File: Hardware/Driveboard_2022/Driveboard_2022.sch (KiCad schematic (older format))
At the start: 10 parts, among them U1 TM4C129E_Launchpad

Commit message: Basically Finished
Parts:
- added Conn? (x12): Molex_SL_03, symbol MRDT_Connectors:Molex_SL_03
- added D? (x7): Blue, symbol Device:LED
- added LED? (x12): Yellow, symbol Device:LED
- added R? (x12): 500, symbol Device:R
- added R? (x7): 330, symbol Device:R
- added SW? (x6): SW_Push, symbol Switch:SW_Push
- added SW?: SW_SPST, symbol Switch:SW_SPST
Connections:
- net +3V3: now also Conn?.1, Conn?.1, Conn?.1, Conn?.1, Conn?.1, Conn?.1, SW?.1, SW?.1, SW?.1, SW?.1, SW?.1, SW?.1, SW?.1 (A)
- net GND: now also Conn?.2, Conn?.2, Conn?.2, Conn?.2, Conn?.2, Conn?.2, Conn?.2, Conn?.2, Conn?.2, Conn?.2, Conn?.2, Conn?.2, D?.1 (K), D?.1 (K), D?.1 (K), D?.1 (K), D?.1 (K), D?.1 (K), D?.1 (K), LED?.1 (K), LED?.1 (K), LED?.1 (K), LED?.1 (K), LED?.1 (K), LED?.1 (K), LED?.1 (K), LED?.1 (K), LED?.1 (K), LED?.1 (K), LED?.1 (K), LED?.1 (K)
- net FLRX: now reaches U1.PC4 (A1_3)
- net FLRX: now also Conn?.3, R?.1
- net FLTX: now reaches U1.PC5 (A1_4)
- net FLTX: now also Conn?.1, R?.1
- net MLRX: now reaches U1.PC6 (A1_5)
- net MLRX: now also Conn?.3, R?.1
- net MLTX: now reaches U1.PC7 (A1_8)
- net MLTX: now also Conn?.1, R?.1
- net BRRX: now reaches U1.PA6 (B1_8)
- net BRRX: now also Conn?.3, R?.1
- net FL_PWM: now reaches U1.PF1 (C1_1)
- net FL_PWM: now also Conn?.3
- net FR_PWM: now reaches U1.PF2 (C1_2)
- net FR_PWM: now also Conn?.3
- net ML_PWM: now reaches U1.PF3 (C1_3)
- net ML_PWM: now also Conn?.3
- net MR_PWM: now reaches U1.PG0 (C1_4)
- net MR_PWM: now also Conn?.3
- net BL_PWM: now reaches U1.PL4 (C1_5)
- net BL_PWM: now also Conn?.3
- net BR_PWM: now reaches U1.PL5 (C1_6)
- net BR_PWM: now also Conn?.3
- net DIR_SWITCH: now reaches U1.PP2 (D1_10)
- net DIR_SWITCH: now also R?.2, SW?.2 (B)
- net FRRX: now reaches U1.PP0 (A2_3)
- net FRRX: now also Conn?.3, R?.1
- net FRTX: now reaches U1.PP1 (A2_4)
- net FRTX: now also Conn?.1, R?.1
- net BLRX: now reaches U1.PA4 (B2_9)
- net BLRX: now also Conn?.3, R?.1
- net BLTX: now reaches U1.PA5 (B2_10)
- net BLTX: now also Conn?.1, R?.1
- net MRRX: now reaches U1.PK0 (B2_5)
- net MRRX: now also Conn?.3, R?.1
- net MRTX: now reaches U1.PK1 (B2_6)
- net MRTX: now also Conn?.1, R?.1
- net FL_DRIVE: now reaches U1.PG1 (C2_1)
- net FL_DRIVE: now also R?.2, SW?.2
- net FR_DRIVE: now reaches U1.PK4 (C2_2)
- net FR_DRIVE: now also R?.2, SW?.2
- net ML_DRIVE: now reaches U1.PK5 (C2_3)
- net ML_DRIVE: now also R?.2, SW?.2
- net MR_DRIVE: now reaches U1.PM0 (C2_4)
- net MR_DRIVE: now also R?.2, SW?.2
- net BL_DRIVE: now reaches U1.PM1 (C2_5)
- net BL_DRIVE: now also R?.2, SW?.2
- net BR_DRIVE: now reaches U1.PM2 (C2_6)
- net BR_DRIVE: now also R?.2, SW?.2
- net BRTX: now reaches U1.PA7 (D2_4)
- net BRTX: now also Conn?.1, R?.1
- new net: LED?.2 (A), R?.2 (x12)
- new net: D?.2 (A), R?.1 (x7)
- no-connect marks 2 -> 49
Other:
- moved on the sheet: LED1, LED2, R1, R2, U1G, U1H

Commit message: I did something guys
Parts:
- added LED? (x5): Blue, symbol Device:LED
- added LED?: Yellow, symbol Device:LED
- added R? (x6): 330, symbol Device:R
- LED? (x12): value Yellow -> Blue
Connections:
- net BL_PWM: now also R?.1
- net BR_PWM: now also R?.1
- net FL_PWM: now also R?.1
- net FR_PWM: now also R?.1
- net GND: now also LED?.1 (K), LED?.1 (K), LED?.1 (K), LED?.1 (K), LED?.1 (K), LED?.1 (K)
- net ML_PWM: now also R?.1
- net MR_PWM: now also R?.1
- new net: LED?.2 (A), R?.2 (x6)

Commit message: I DID MORE SHIT
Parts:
- added LED? (x6): Red, symbol Device:LED
- added R? (x6): 330, symbol Device:R
- LED?: value Yellow -> Blue
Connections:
- net GND: now also LED?.1 (K), LED?.1 (K), LED?.1 (K), LED?.1 (K), LED?.1 (K), LED?.1 (K)
- new net: LED?.2 (A), R?.2 (x6)
- new net BL_FLT: R?.1
- new net BR_FLT: R?.1
- new net FL_FLT: R?.1
- new net FR_FLT: R?.1
- new net ML_FLT: R?.1
- new net MR_FLT: R?.1

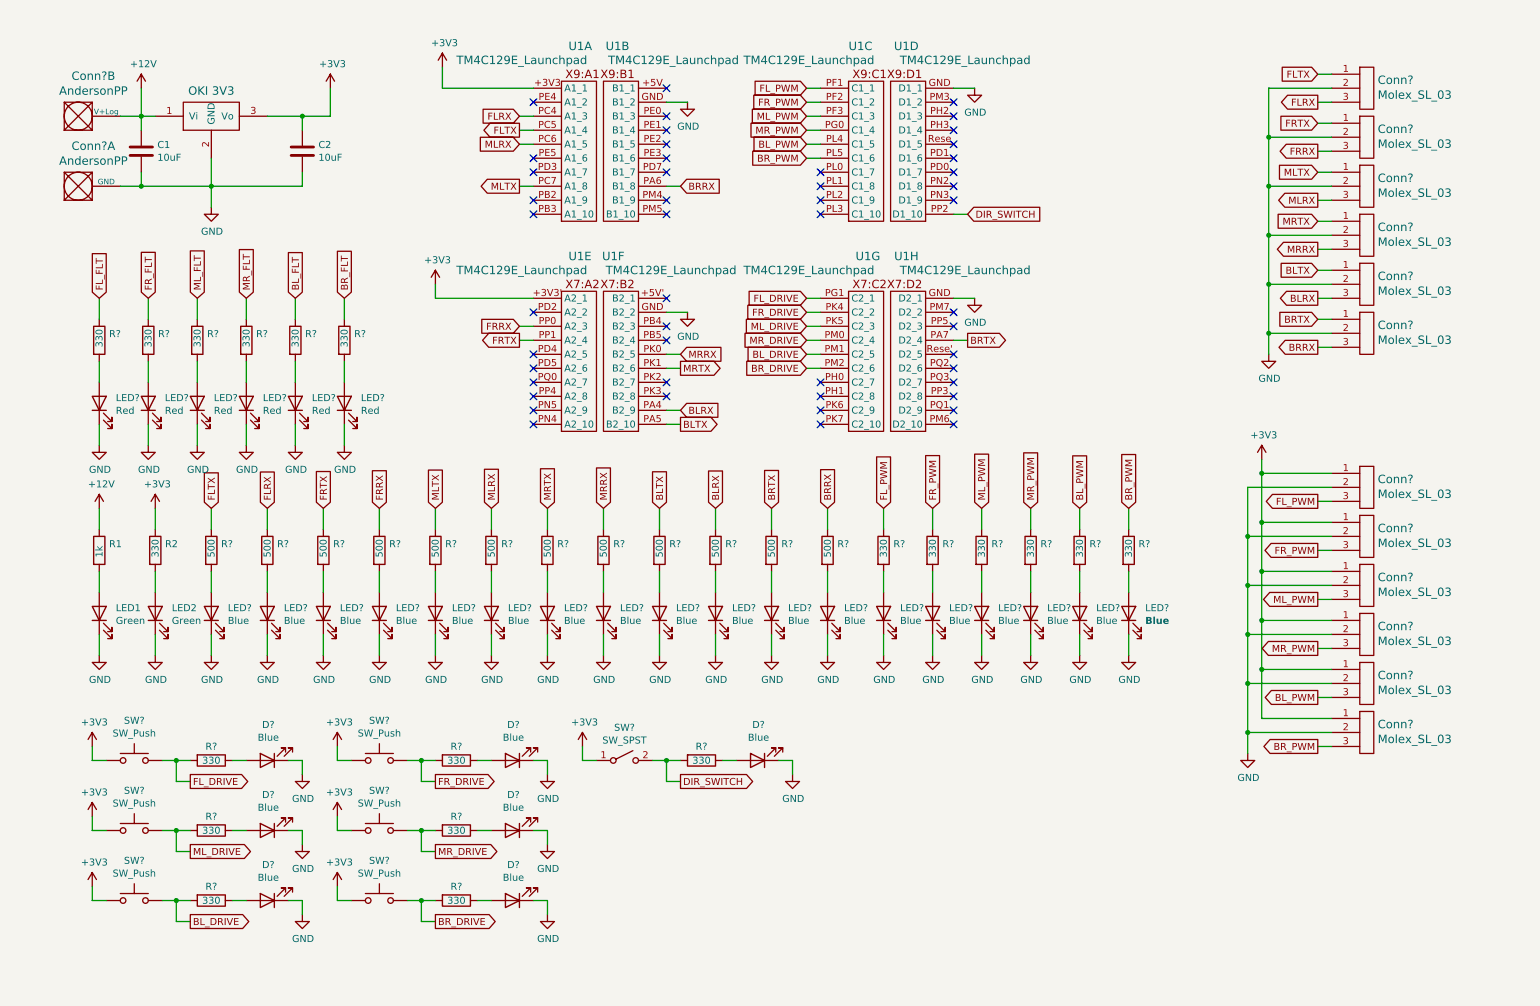
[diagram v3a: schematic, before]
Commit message: Added Fault LEDs, and Adjusted Placement
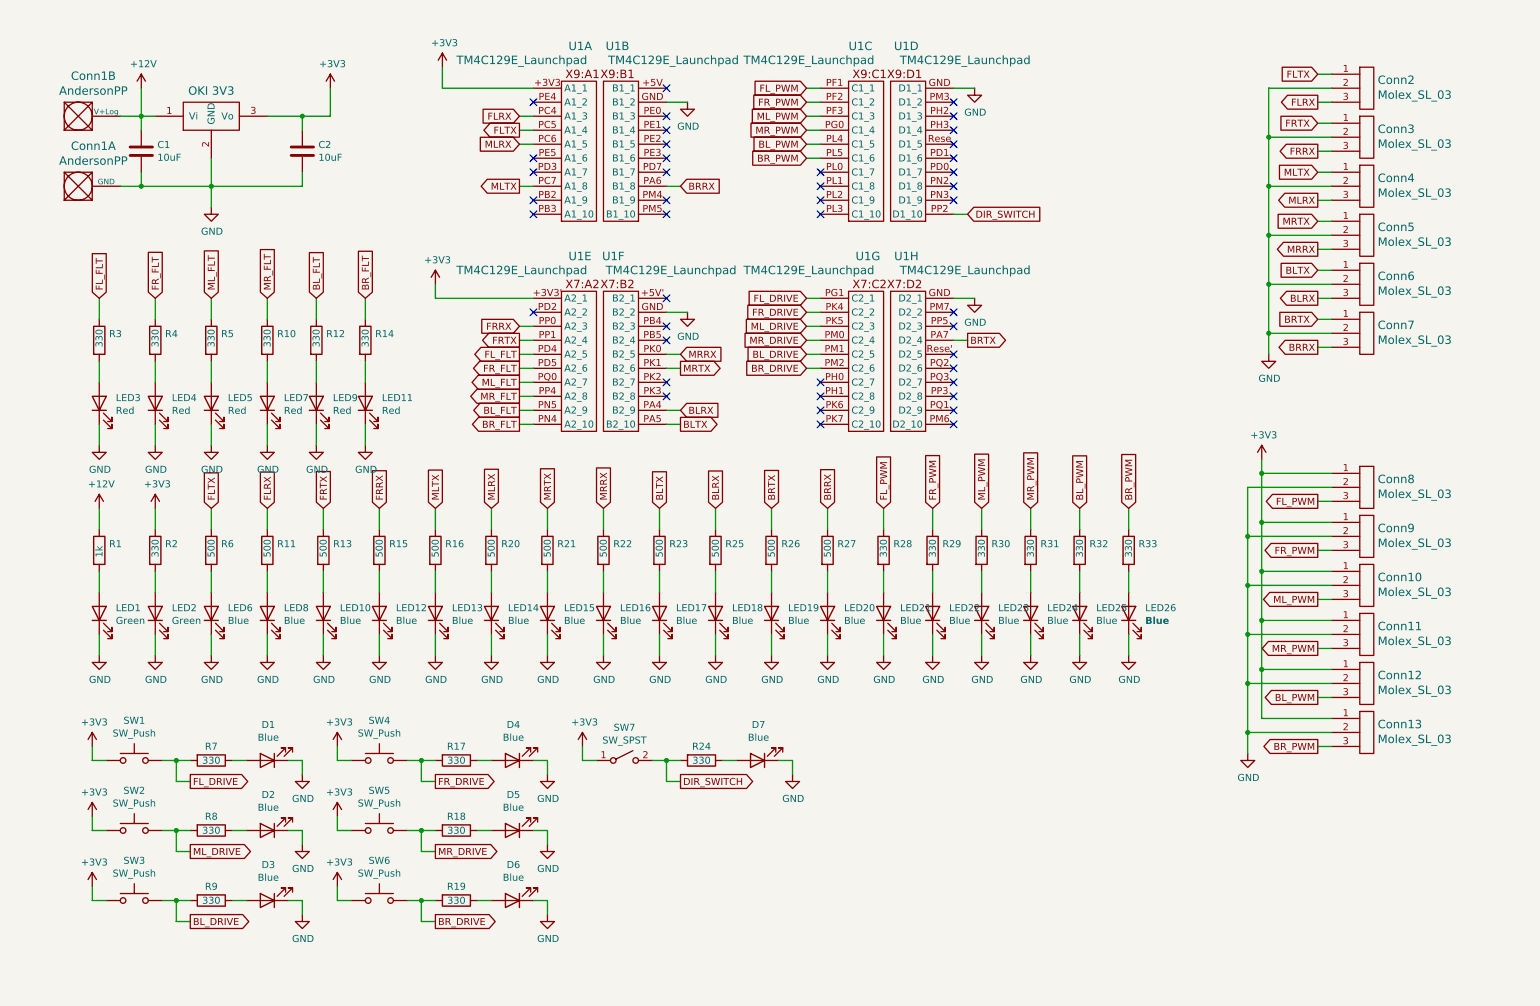
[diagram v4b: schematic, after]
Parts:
- removed R?: 330, symbol Device:R
- added R3: 330, symbol Device:R
- gave numbers to parts that had none: 82
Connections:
- net BL_FLT: now also U1.PN5 (A2_9)
- net BR_FLT: now also U1.PN4 (A2_10)
- net FL_FLT: now also U1.PD4 (A2_5), R3.1
- net FR_FLT: now also U1.PD5 (A2_6)
- net ML_FLT: now also U1.PQ0 (A2_7)
- net MR_FLT: now also U1.PP4 (A2_8)
- net at LED3.2 (A): now also R3.2
- no-connect marks 49 -> 43
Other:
- moved on the sheet: LED11, LED4, LED5, LED7, LED9, R10, R12, R14, R4, R5

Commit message: Microfit YASSS~
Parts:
- removed Conn2, Conn3, Conn4, Conn5, Conn6, Conn7: Molex_SL_03, symbol MRDT_Connectors:Molex_SL_03
- added Conn? (x6): Molex_uF_S_03, MRDT_Connectors:MOLEX_uF_S_03_Horizontal, symbol MRDT_Connectors:Molex_uF_S_03
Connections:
- net BLRX: now also Conn?.3
- net BLTX: now also Conn?.1
- net BRRX: now also Conn?.3
- net BRTX: now also Conn?.1
- net FLRX: now also Conn?.3
- net FLTX: now also Conn?.1
- net FRRX: now also Conn?.3
- net FRTX: now also Conn?.1
- net GND: now also Conn?.2, Conn?.2, Conn?.2, Conn?.2, Conn?.2, Conn?.2
- net MLRX: now also Conn?.3
- net MLTX: now also Conn?.1
- net MRRX: now also Conn?.3
- net MRTX: now also Conn?.1
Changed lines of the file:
@@
 NoConn ~ 5050 1050
 NoConn ~ 5050 2550
-$Comp
-L MRDT_Connectors:Molex_SL_03 Conn2
-U 1 1 614D2718
-P 10000 1200
-F 0 "Conn2" H 10128 1408 60  0000 L CNN
-F 1 "Molex_SL_03" H 10128 1302 60  0000 L CNN
-F 2 "" H 10000 1200 60  0001 C CNN
-F 3 "" H 10000 1200 60  0001 C CNN
-	1    10000 1200
-	1    0    0    -1
-$EndComp
-$Comp
-L MRDT_Connectors:Molex_SL_03 Conn3
-U 1 1 614D38EC
-P 10000 1550
-F 0 "Conn3" H 10128 1758 60  0000 L CNN
-F 1 "Molex_SL_03" H 10128 1652 60  0000 L CNN
-F 2 "" H 10000 1550 60  0001 C CNN
-F 3 "" H 10000 1550 60  0001 C CNN
-	1    10000 1550
-	1    0    0    -1
-$EndComp
-$Comp
-L MRDT_Connectors:Molex_SL_03 Conn4
-U 1 1 614D3D09
-P 10000 1900
-F 0 "Conn4" H 10128 2108 60  0000 L CNN
-F 1 "Molex_SL_03" H 10128 2002 60  0000 L CNN
-F 2 "" H 10000 1900 60  0001 C CNN
-F 3 "" H 10000 1900 60  0001 C CNN
-	1    10000 1900
-	1    0    0    -1
-$EndComp
-$Comp
-L MRDT_Connectors:Molex_SL_03 Conn5
-U 1 1 614D41F2
-P 10000 2250
-F 0 "Conn5" H 10128 2458 60  0000 L CNN
-F 1 "Molex_SL_03" H 10128 2352 60  0000 L CNN
-F 2 "" H 10000 2250 60  0001 C CNN
-F 3 "" H 10000 2250 60  0001 C CNN
-	1    10000 2250
-	1    0    0    -1
-$EndComp
-$Comp
-L MRDT_Connectors:Molex_SL_03 Conn6
-U 1 1 614D475B
-P 10000 2600
-F 0 "Conn6" H 10128 2808 60  0000 L CNN
-F 1 "Molex_SL_03" H 10128 2702 60  0000 L CNN
-F 2 "" H 10000 2600 60  0001 C CNN
-F 3 "" H 10000 2600 60  0001 C CNN
-	1    10000 2600
-	1    0    0    -1
-$EndComp
-$Comp
-L MRDT_Connectors:Molex_SL_03 Conn7
-U 1 1 614D4EE0
-P 10000 2950
-F 0 "Conn7" H 10128 3158 60  0000 L CNN
-F 1 "Molex_SL_03" H 10128 3052 60  0000 L CNN
-F 2 "" H 10000 2950 60  0001 C CNN
-F 3 "" H 10000 2950 60  0001 C CNN
-	1    10000 2950
-	1    0    0    -1
-$EndComp
 Text GLabel 9700 950  0    50   Input ~ 0
 FLTX
@@
 	1    0    0    -1
 $EndComp
+$Comp
+L MRDT_Connectors:Molex_uF_S_03 Conn?
+U 1 1 61984A08
+P 10000 1200
+F 0 "Conn?" H 10128 1408 60  0000 L CNN
+F 1 "Molex_uF_S_03" H 10128 1302 60  0000 L CNN
+F 2 "MRDT_Connectors:MOLEX_uF_S_03_Horizontal" H 10000 1200 60  0001 C CNN
+F 3 "" H 10000 1200 60  0001 C CNN
+	1    10000 1200
+	1    0    0    -1
+$EndComp
+$Comp
+L MRDT_Connectors:Molex_uF_S_03 Conn?
+U 1 1 619BB189
+P 10000 1550
+F 0 "Conn?" H 10128 1758 60  0000 L CNN
+F 1 "Molex_uF_S_03" H 10128 1652 60  0000 L CNN
+F 2 "MRDT_Connectors:MOLEX_uF_S_03_Horizontal" H 10000 1550 60  0001 C CNN
+F 3 "" H 10000 1550 60  0001 C CNN
+	1    10000 1550
+	1    0    0    -1
+$EndComp
+$Comp
+L MRDT_Connectors:Molex_uF_S_03 Conn?
+U 1 1 619CC8AC
+P 10000 1900
+F 0 "Conn?" H 10128 2108 60  0000 L CNN
+F 1 "Molex_uF_S_03" H 10128 2002 60  0000 L CNN
+F 2 "MRDT_Connectors:MOLEX_uF_S_03_Horizontal" H 10000 1900 60  0001 C CNN
+F 3 "" H 10000 1900 60  0001 C CNN
+	1    10000 1900
+	1    0    0    -1
+$EndComp
+$Comp
+L MRDT_Connectors:Molex_uF_S_03 Conn?
+U 1 1 619DE023
+P 10000 2250
+F 0 "Conn?" H 10128 2458 60  0000 L CNN
+F 1 "Molex_uF_S_03" H 10128 2352 60  0000 L CNN
+F 2 "MRDT_Connectors:MOLEX_uF_S_03_Horizontal" H 10000 2250 60  0001 C CNN
+F 3 "" H 10000 2250 60  0001 C CNN
+	1    10000 2250
+	1    0    0    -1
+$EndComp
+$Comp
+L MRDT_Connectors:Molex_uF_S_03 Conn?
+U 1 1 619EF87F
+P 10000 2600
+F 0 "Conn?" H 10128 2808 60  0000 L CNN
+F 1 "Molex_uF_S_03" H 10128 2702 60  0000 L CNN
+F 2 "MRDT_Connectors:MOLEX_uF_S_03_Horizontal" H 10000 2600 60  0001 C CNN
+F 3 "" H 10000 2600 60  0001 C CNN
+	1    10000 2600
+	1    0    0    -1
+$EndComp
+$Comp
+L MRDT_Connectors:Molex_uF_S_03 Conn?
+U 1 1 61A01123
+P 10000 2950
+F 0 "Conn?" H 10128 3158 60  0000 L CNN
+F 1 "Molex_uF_S_03" H 10128 3052 60  0000 L CNN
+F 2 "MRDT_Connectors:MOLEX_uF_S_03_Horizontal" H 10000 2950 60  0001 C CNN
+F 3 "" H 10000 2950 60  0001 C CNN
+	1    10000 2950
+	1    0    0    -1
+$EndComp

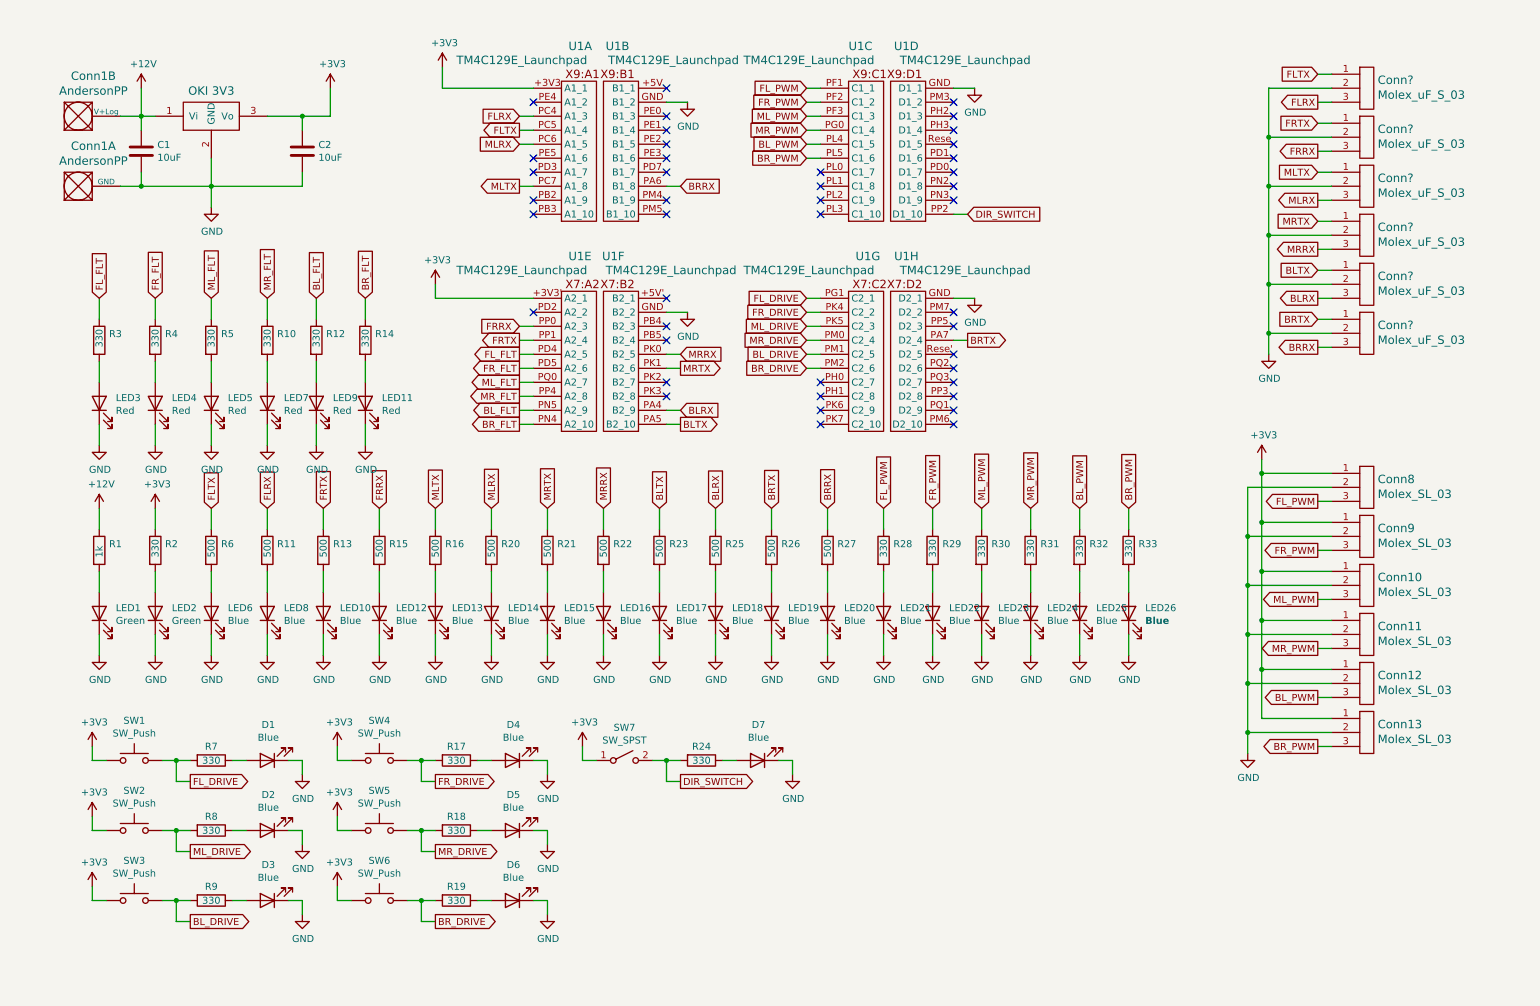
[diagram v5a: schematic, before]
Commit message: Organization for BoardA
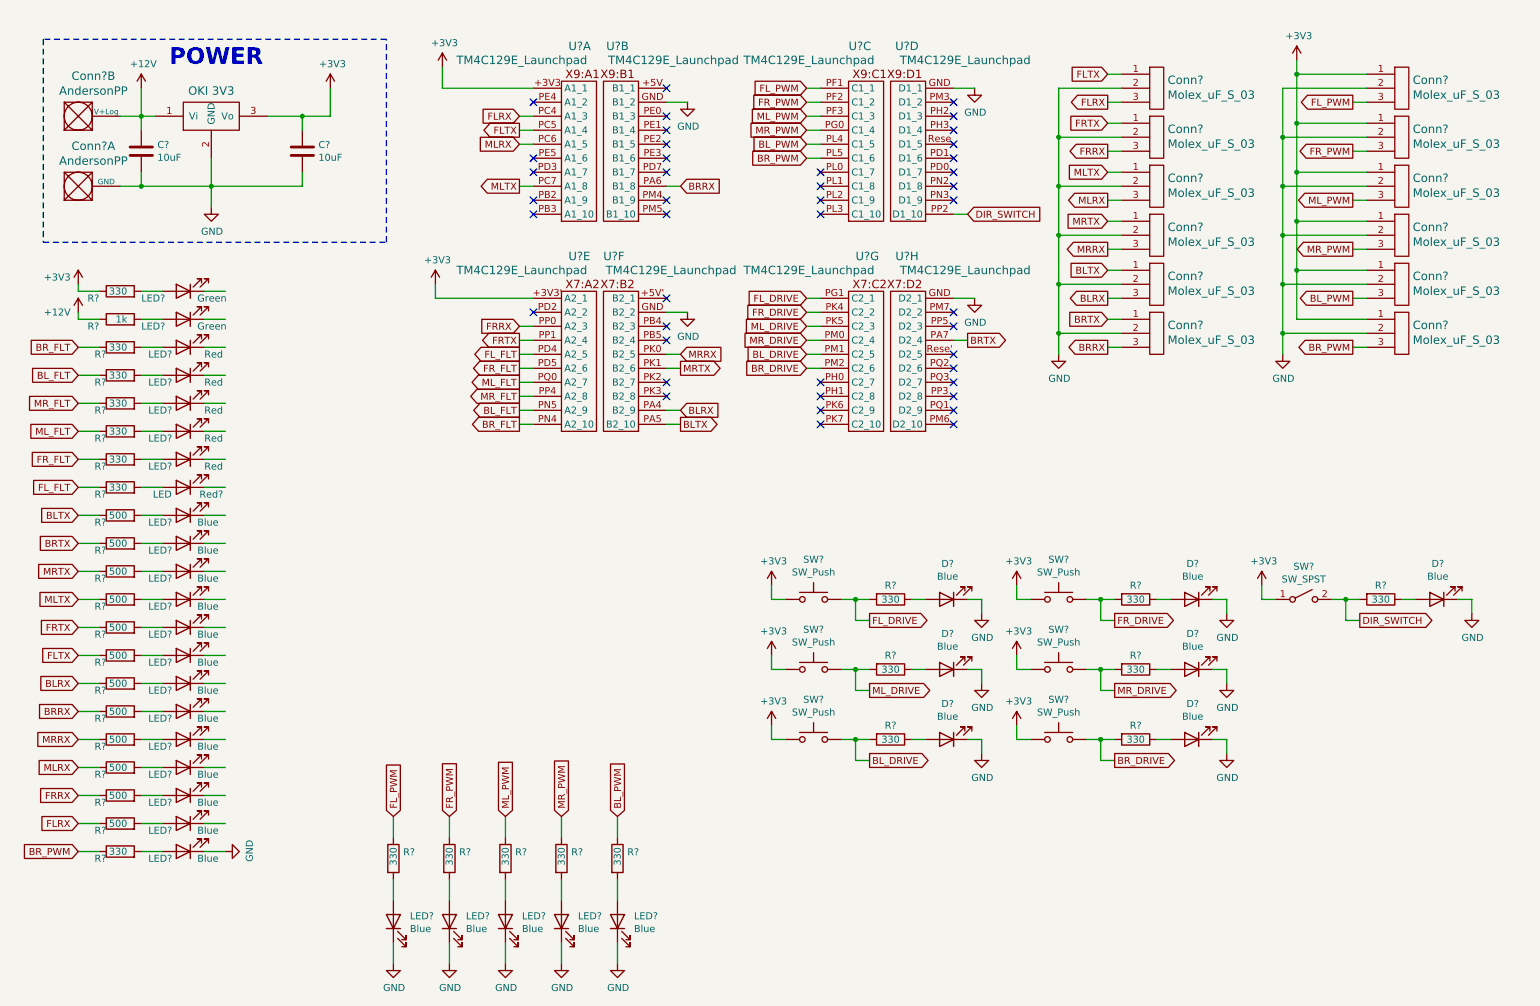
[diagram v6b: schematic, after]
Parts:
- removed Conn10, Conn11, Conn12, Conn13, Conn8, Conn9: Molex_SL_03, symbol MRDT_Connectors:Molex_SL_03
- removed LED3: Red, symbol Device:LED
- added Conn? (x6): Molex_uF_S_03, MRDT_Connectors:MOLEX_uF_S_03_Horizontal, symbol MRDT_Connectors:Molex_uF_S_03
- added Red?: LED, symbol Device:LED
- renumbered C1 to C?, C2 to C?, Conn1 to Conn?, D1 to D?, D2 to D?, D3 to D?, D4 to D?, D5 to D?, D6 to D?, D7 to D?, LED1 to LED?, LED2 to LED?, LED21 to LED?, LED22 to LED?, LED23 to LED?, LED6 to LED?, LED24 to LED?, LED25 to LED?, LED8 to LED?, LED26 to LED?, LED10 to LED?, LED12 to LED?, LED13 to LED?, LED14 to LED?, LED15 to LED?, LED16 to LED?, LED17 to LED?, LED18 to LED?, LED19 to LED?, LED20 to LED?, LED11 to LED?, LED9 to LED?, LED7 to LED?, LED5 to LED?, LED4 to LED?, R1 to R?, R2 to R?, R28 to R?, R29 to R?, R30 to R?, R6 to R?, R11 to R?, R13 to R?, R15 to R?, R31 to R?, R16 to R?, R20 to R?, R21 to R?, R22 to R?, R23 to R?, R25 to R?, R32 to R?, R26 to R?, R27 to R?, R33 to R?, R7 to R?, R8 to R?, R9 to R?, R17 to R?, R18 to R?, R19 to R?, R24 to R?, R14 to R?, R12 to R?, R10 to R?, R5 to R?, R4 to R?, R3 to R?, SW1 to SW?, SW2 to SW?, SW3 to SW?, SW4 to SW?, SW5 to SW?, SW6 to SW?, SW7 to SW?, U2 to U?, U1 to U?
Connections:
- wire segments 249 -> 251
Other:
- note added: "POWER"
- moved on the sheet: Conn?, D?, LED?, R?, SW?
